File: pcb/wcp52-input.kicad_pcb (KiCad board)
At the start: 4 copper layers, 48.5 x 30.5 mm, 77 parts, among them J1 5V, J3 IN1, J4 IN2, J5 CTRL, J6 PHASEREF, J7 5V, Q1 PMV160UP, Q2 2N7002, Q3 MMBT3906, Q4 2N7002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

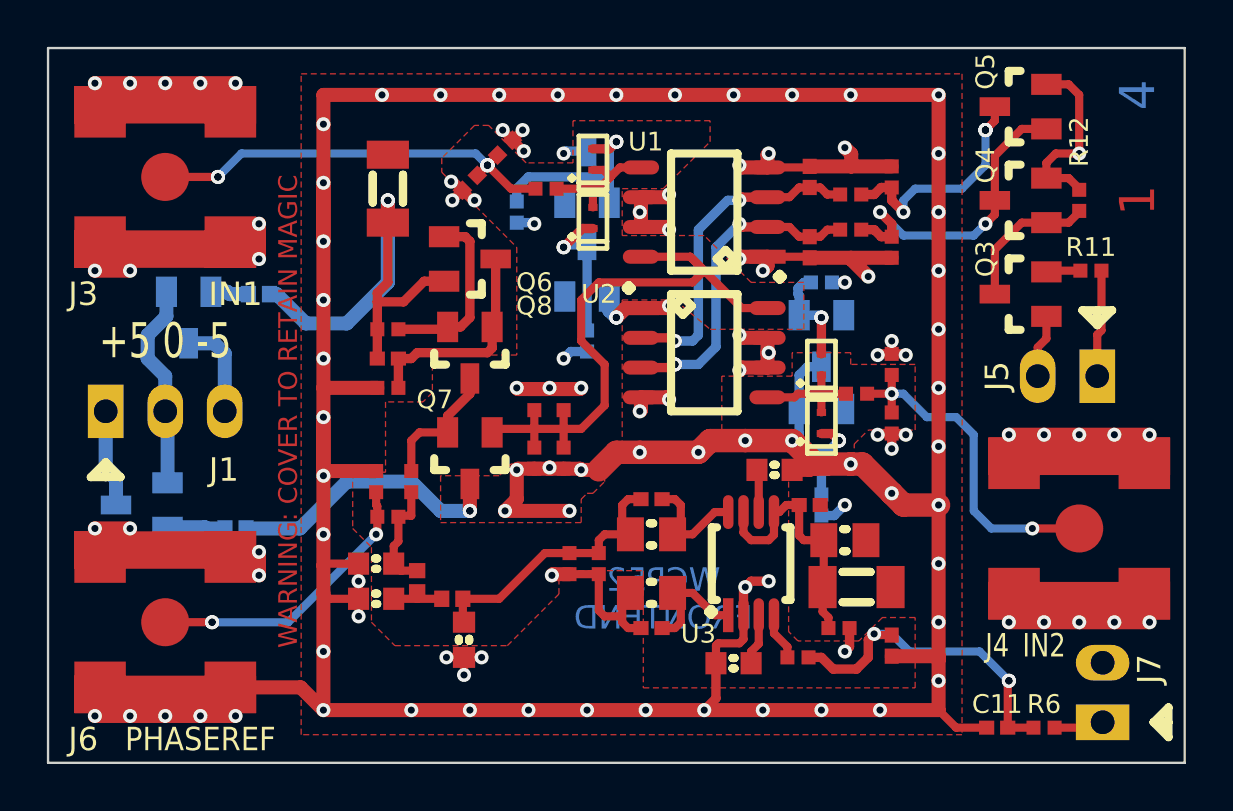
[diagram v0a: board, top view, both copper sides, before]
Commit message: Added more decoupling
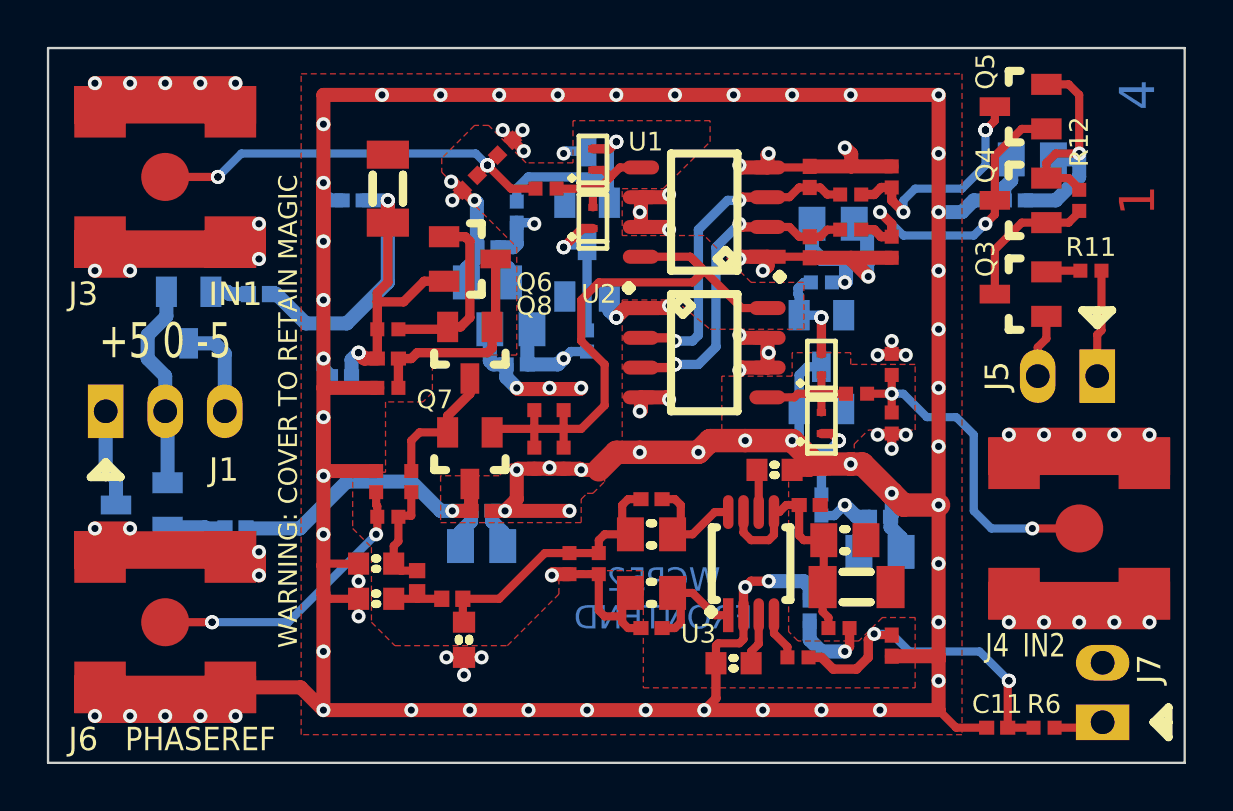
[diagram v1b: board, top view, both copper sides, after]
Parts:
- added C1: 1n, IPC7351-Nominal:CAPC1005X55, F.Cu at (105.5, 79.2)
- added C20: 1n, IPC7351-Nominal:CAPC1005X55, B.Cu at (128.2, 66.0)
- added C21: 1n, IPC7351-Nominal:CAPC1005X55, B.Cu at (122.5, 79.5)
- added C22: 1n, IPC7351-Nominal:CAPC1005X55, B.Cu at (99.5, 73.5)
- added C23: 1n, IPC7351-Nominal:CAPC1005X55, B.Cu at (119.5, 83.5)
- added C24: 1n, IPC7351-Nominal:CAPC1005X55, B.Cu at (100.0, 66.0)
- added C25: 1n, IPC7351-Nominal:CAPC1005X55, B.Cu at (105.5, 79.2)
- added C26: 1n, IPC7351-Nominal:CAPC1005X55, B.Cu at (105.8, 68.0)
- added C27: 1n, IPC7351-Nominal:CAPC1005X55, B.Cu at (107.0, 73.0)
- added C28: 1n, IPC7351-Nominal:CAPC1005X55, B.Cu at (121.5, 68.5)
- added C29: 220n, IPC7351-Nominal:CAPC2012X70, B.Cu at (105.5, 80.8)
- added C30: 220n, IPC7351-Nominal:CAPC2012X70, B.Cu at (129.0, 64.2)
- added C31: 220n, IPC7351-Nominal:CAPC2012X70, B.Cu at (106.8, 71.5)
- added C32: 220n, IPC7351-Nominal:CAPC2012X70, B.Cu at (120.5, 67.0)
- added C33: 220n, IPC7351-Nominal:CAPC2012X70, B.Cu at (122.5, 81.0)
- added C34: 220n, IPC7351-Nominal:CAPC2012X70, B.Cu at (105.8, 69.5)
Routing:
- net GND: track 297.1 -> 321.7 mm
- net -5: track 29.2 -> 44.4 mm, vias 5 -> 7
- net +5: track 15.4 -> 26.7 mm, vias 5 -> 4
